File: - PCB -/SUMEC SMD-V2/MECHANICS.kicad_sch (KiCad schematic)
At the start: 8 parts, among them J1 Conn_01x04_Pin, SW1 SW_Push, SW4 SW_DPDT_x2

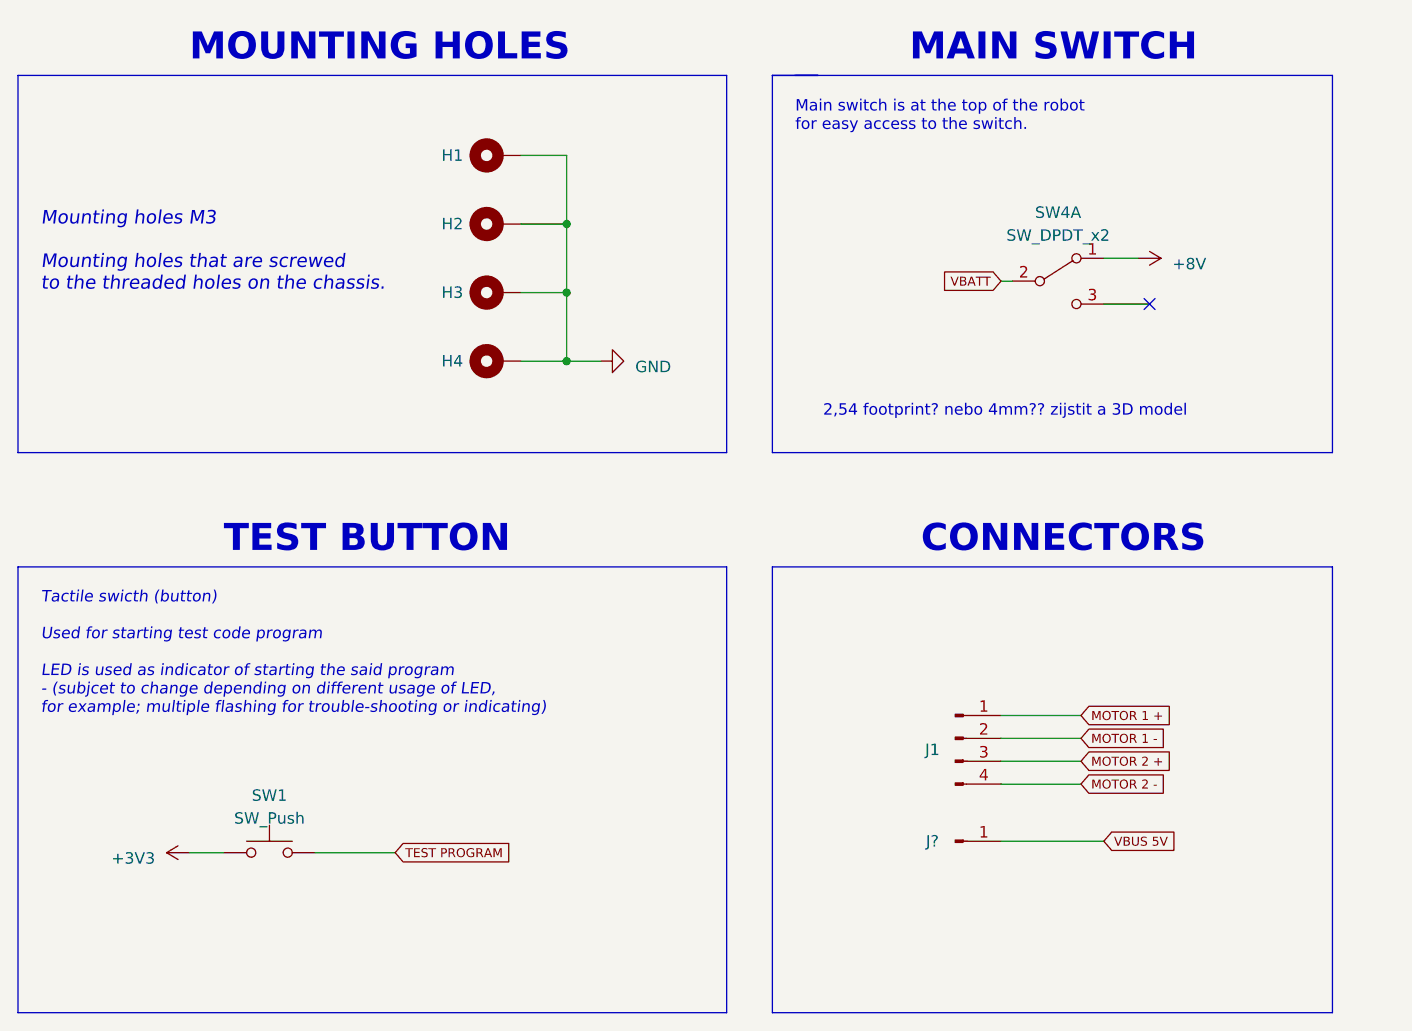
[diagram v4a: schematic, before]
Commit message: Updates:
GyroScope project file, QRE1113 Board update and BOM, SMDv2 iBOM and schematic update.
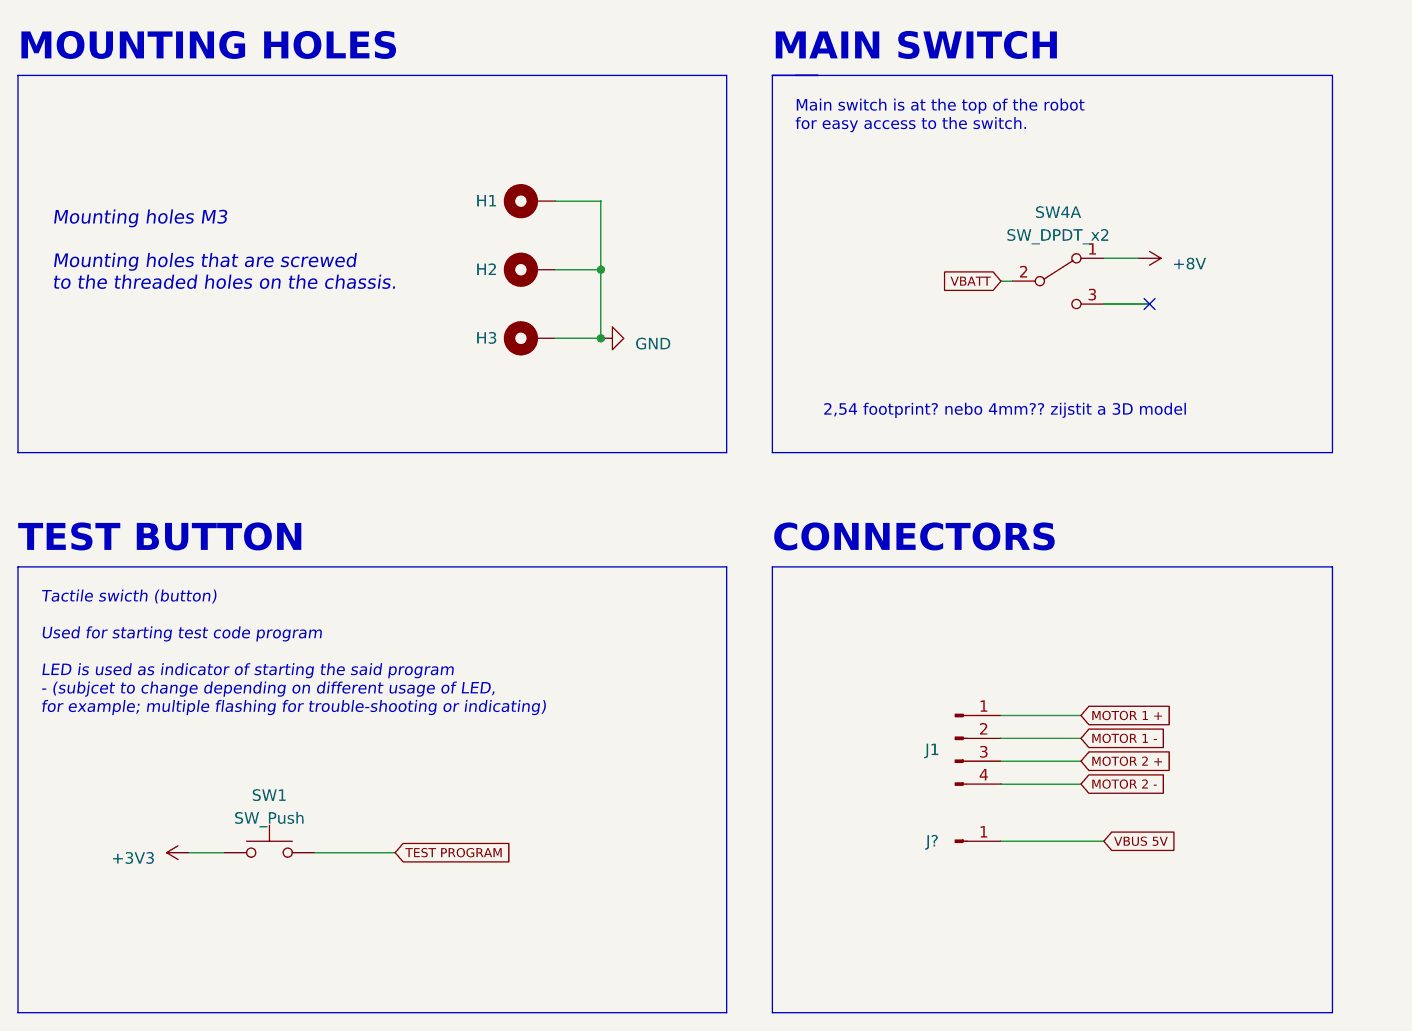
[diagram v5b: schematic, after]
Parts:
- removed H4: MountingHole_Pad, MountingHole:MountingHole_3.2mm_M3_Pad, symbol Mechanical:MountingHole_Pad
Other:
- moved on the sheet: H1, H2, H3
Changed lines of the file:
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@@
     (company "SPŠ NA PROSEKU")
   )
-  (junction (at 125.73 68.58) (diameter 0) (color 0 0 0 0)
-  )
-  (junction (at 125.73 60.96) (diameter 0) (color 0 0 0 0)
-  )
-  (junction (at 125.73 76.2) (diameter 0) (color 0 0 0 0)
+  (junction (at 129.54 73.66) (diameter 0) (color 0 0 0 0)
+  )
+  (junction (at 129.54 66.04) (diameter 0) (color 0 0 0 0)
   )
   (no_connect (at 190.5 69.85))
@@
     (stroke (width 0) (type default))
   )
-  (wire (pts (xy 120.65 76.2) (xy 125.73 76.2))
-    (stroke (width 0) (type default))
-  )
-  (wire (pts (xy 125.73 76.2) (xy 125.73 68.58))
-    (stroke (width 0) (type default))
-  )
-  (wire (pts (xy 120.65 53.34) (xy 125.73 53.34))
+  (wire (pts (xy 124.46 58.42) (xy 129.54 58.42))
     (stroke (width 0) (type default))
   )
@@
     (stroke (width 0) (type default))
   )
-  (wire (pts (xy 125.73 60.96) (xy 125.73 68.58))
+  (wire (pts (xy 129.54 66.04) (xy 129.54 73.66))
     (stroke (width 0) (type default))
   )
@@
     (stroke (width 0) (type default))
   )
-  (wire (pts (xy 125.73 68.58) (xy 120.65 68.58))
+  (wire (pts (xy 129.54 73.66) (xy 124.46 73.66))
     (stroke (width 0) (type default))
   )
@@
     (stroke (width 0) (type default))
   )
-  (wire (pts (xy 125.73 76.2) (xy 129.54 76.2))
-    (stroke (width 0) (type default))
-  )
   (polyline (pts (xy 210.82 99.06) (xy 210.82 148.59))
     (stroke (width 0) (type default))
@@
     (stroke (width 0) (type default))
   )
-  (wire (pts (xy 120.65 60.96) (xy 125.73 60.96))
+  (wire (pts (xy 124.46 66.04) (xy 129.54 66.04))
     (stroke (width 0) (type default))
   )
@@
     (stroke (width 0) (type default))
   )
-  (wire (pts (xy 125.73 53.34) (xy 125.73 60.96))
+  (wire (pts (xy 129.54 58.42) (xy 129.54 66.04))
     (stroke (width 0) (type default))
   )
@@
     (stroke (width 0) (type default))
   )
-  (text "MOUNTING HOLES" (at 83.82 43.18 0)
+  (text "MOUNTING HOLES" (at 64.77 43.18 0)
     (effects (font (size 3 3) bold (color 0 0 0 1)) (justify left bottom))
   )
   (text "Mounting holes M3 \n\nMounting holes that are screwed \nto the threaded holes on the chassis.\n"
-    (at 67.31 68.58 0)
+    (at 68.58 68.58 0)
     (effects (font (size 1.5 1.5) italic) (justify left bottom))
   )
-  (text "MAIN SWITCH" (at 163.83 43.18 0)
+  (text "MAIN SWITCH" (at 148.59 43.18 0)
     (effects (font (size 3 3) bold (color 0 0 0 1)) (justify left bottom))
   )
-  (text "TEST BUTTON" (at 87.63 97.79 0)
+  (text "TEST BUTTON" (at 64.77 97.79 0)
     (effects (font (size 3 3) bold (color 0 0 0 1)) (justify left bottom))
   )
@@
     (effects (font (size 1.27 1.27)) (justify left bottom))
   )
-  (text "CONNECTORS" (at 165.1 97.79 0)
+  (text "CONNECTORS" (at 148.59 97.79 0)
     (effects (font (size 3 3) bold (color 0 0 0 1)) (justify left bottom))
   )
@@
     )
   )
-  (symbol (lib_id "power:GND") (at 129.54 76.2 90) (unit 1)
+  (symbol (lib_id "power:GND") (at 129.54 73.66 90) (unit 1)
     (in_bom yes) (on_board yes) (dnp no) (fields_autoplaced)
-    (property "Reference" "#PWR026" (at 135.89 76.2 0)
-      (effects (font (size 1.27 1.27)) hide)
-    )
-    (property "Value" "GND" (at 133.35 76.835 90)
+    (property "Reference" "#PWR026" (at 135.89 73.66 0)
+      (effects (font (size 1.27 1.27)) hide)
+    )
+    (property "Value" "GND" (at 133.35 74.295 90)
       (effects (font (size 1.27 1.27)) (justify right))
     )
-    (property "Footprint" "" (at 129.54 76.2 0)
-      (effects (font (size 1.27 1.27)) hide)
-    )
-    (property "Datasheet" "" (at 129.54 76.2 0)
+    (property "Footprint" "" (at 129.54 73.66 0)
+      (effects (font (size 1.27 1.27)) hide)
+    )
+    (property "Datasheet" "" (at 129.54 73.66 0)
       (effects (font (size 1.27 1.27)) hide)
     )
@@
     )
   )
-  (symbol (lib_id "Mechanical:MountingHole_Pad") (at 118.11 76.2 90) (unit 1)
-    (in_bom yes) (on_board yes) (dnp no)
-    (property "Reference" "H4" (at 113.03 76.2 90)
-      (effects (font (size 1.27 1.27)))
-    )
-    (property "Value" "MountingHole_Pad" (at 116.84 73.66 90)
-      (effects (font (size 1.27 1.27)) hide)
-    )
-    (property "Footprint" "MountingHole:MountingHole_3.2mm_M3_Pad" (at 118.11 76.2 0)
-      (effects (font (size 1.27 1.27)) hide)
-    )
-    (property "Datasheet" "~" (at 118.11 76.2 0)
-      (effects (font (size 1.27 1.27)) hide)
-    )
-    (pin "1")
-    (instances
-      (project "sumec"
-        (path "/fc70a1a8-ed7c-4a0f-9b1a-f23293528385/05a35bad-c108-46ad-8f95-76319a60a14f"
-          (reference "H4") (unit 1)
-        )
-      )
-    )
-  )
   (symbol (lib_id "Connector:Conn_01x01_Pin") (at 168.91 129.54 0) (unit 1)
     (in_bom yes) (on_board yes) (dnp no)
@@
     )
   )
-  (symbol (lib_id "Mechanical:MountingHole_Pad") (at 118.11 53.34 90) (unit 1)
-    (in_bom yes) (on_board yes) (dnp no)
-    (property "Reference" "H1" (at 113.03 53.34 90)
-      (effects (font (size 1.27 1.27)))
-    )
-    (property "Value" "MountingHole_Pad" (at 116.84 50.8 90)
-      (effects (font (size 1.27 1.27)) hide)
-    )
-    (property "Footprint" "MountingHole:MountingHole_3.2mm_M3_Pad" (at 118.11 53.34 0)
-      (effects (font (size 1.27 1.27)) hide)
-    )
-    (property "Datasheet" "~" (at 118.11 53.34 0)
+  (symbol (lib_id "Mechanical:MountingHole_Pad") (at 121.92 58.42 90) (unit 1)
+    (in_bom yes) (on_board yes) (dnp no)
+    (property "Reference" "H1" (at 116.84 58.42 90)
+      (effects (font (size 1.27 1.27)))
+    )
+    (property "Value" "MountingHole_Pad" (at 120.65 55.88 90)
+      (effects (font (size 1.27 1.27)) hide)
+    )
+    (property "Footprint" "MountingHole:MountingHole_3.2mm_M3_Pad" (at 121.92 58.42 0)
+      (effects (font (size 1.27 1.27)) hide)
+    )
+    (property "Datasheet" "~" (at 121.92 58.42 0)
       (effects (font (size 1.27 1.27)) hide)
     )
@@
     )
   )
-  (symbol (lib_id "Mechanical:MountingHole_Pad") (at 118.11 60.96 90) (unit 1)
-    (in_bom yes) (on_board yes) (dnp no)
-    (property "Reference" "H2" (at 113.03 60.96 90)
-      (effects (font (size 1.27 1.27)))
-    )
-    (property "Value" "MountingHole_Pad" (at 116.84 58.42 90)
-      (effects (font (size 1.27 1.27)) hide)
-    )
-    (property "Footprint" "MountingHole:MountingHole_3.2mm_M3_Pad" (at 118.11 60.96 0)
-      (effects (font (size 1.27 1.27)) hide)
-    )
-    (property "Datasheet" "~" (at 118.11 60.96 0)
+  (symbol (lib_id "Mechanical:MountingHole_Pad") (at 121.92 66.04 90) (unit 1)
+    (in_bom yes) (on_board yes) (dnp no)
+    (property "Reference" "H2" (at 116.84 66.04 90)
+      (effects (font (size 1.27 1.27)))
+    )
+    (property "Value" "MountingHole_Pad" (at 120.65 63.5 90)
+      (effects (font (size 1.27 1.27)) hide)
+    )
+    (property "Footprint" "MountingHole:MountingHole_3.2mm_M3_Pad" (at 121.92 66.04 0)
+      (effects (font (size 1.27 1.27)) hide)
+    )
+    (property "Datasheet" "~" (at 121.92 66.04 0)
       (effects (font (size 1.27 1.27)) hide)
     )
@@
     )
   )
-  (symbol (lib_id "Mechanical:MountingHole_Pad") (at 118.11 68.58 90) (unit 1)
-    (in_bom yes) (on_board yes) (dnp no)
-    (property "Reference" "H3" (at 113.03 68.58 90)
-      (effects (font (size 1.27 1.27)))
-    )
-    (property "Value" "MountingHole_Pad" (at 116.84 66.04 90)
-      (effects (font (size 1.27 1.27)) hide)
-    )
-    (property "Footprint" "MountingHole:MountingHole_3.2mm_M3_Pad" (at 118.11 68.58 0)
-      (effects (font (size 1.27 1.27)) hide)
-    )
-    (property "Datasheet" "~" (at 118.11 68.58 0)
-      (effects (font (size 1.27 1.27)) hide)
-    )
+  (symbol (lib_id "Mechanical:MountingHole_Pad") (at 121.92 73.66 90) (unit 1)
+    (in_bom yes) (on_board yes) (dnp no)
+    (property "Reference" "H3" (at 116.84 73.66 90)
+      (effects (font (size 1.27 1.27)))
+    )
+    (property "Value" "MountingHole_Pad" (at 120.65 71.12 90)
+      (effects (font (size 1.27 1.27)) hide)
+    )
+    (property "Footprint" "MountingHole:MountingHole_3.2mm_M3_Pad" (at 121.92 73.66 0)
+      (effects (font (size 1.27 1.27)) hide)
+    )
+    (property "Datasheet" "~" (at 121.92 73.66 0)
+      (effects (font (size 1.27 1.27)) hide)
+    )

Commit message: SMDv2 Schematic update
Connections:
- net MOTOR 1 + renamed OUT 1A
- net MOTOR 1 - renamed OUT 1B
- net MOTOR 2 + renamed OUT 2A
- net MOTOR 2 - renamed OUT 2B
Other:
- note added: "4mm custom footprint"
- note removed: "2,54 footprint? nebo 4mm?? zijstit a 3D model"
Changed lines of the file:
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@@
+    (stroke (width 0) (type default))
+  )
+  (wire (pts (xy 132.08 73.66) (xy 129.54 73.66))
     (stroke (width 0) (type default))
   )
@@
     (stroke (width 0) (type default))
   )
-  (wire (pts (xy 185.42 129.54) (xy 173.99 129.54))
+  (wire (pts (xy 182.88 129.54) (xy 173.99 129.54))
     (stroke (width 0) (type default))
   )
@@
     (effects (font (size 1.27 1.27) italic) (justify left bottom))
   )
-  (text " 2,54 footprint? nebo 4mm?? zijstit a 3D model" (at 153.67 82.55 0)
+  (text " 4mm custom footprint" (at 167.64 78.74 0)
     (effects (font (size 1.27 1.27) (color 255 0 0 1)) (justify left bottom))
   )
-  (global_label "VBUS 5V" (shape input) (at 185.42 129.54 0) (fields_autoplaced)
+  (global_label "OUT 2B" (shape input) (at 182.88 123.19 0) (fields_autoplaced)
     (effects (font (size 1 1) (color 0 0 0 1)) (justify left))
-    (property "Intersheetrefs" "${INTERSHEET_REFS}" (at 194.1364 129.54 0)
+    (property "Intersheetrefs" "${INTERSHEET_REFS}" (at 190.7393 123.19 0)
       (effects (font (size 1.27 1.27)) (justify left) hide)
     )
   )
-  (global_label "MOTOR 2 -" (shape input) (at 182.88 123.19 0) (fields_autoplaced)
+  (global_label "VBUS 5V" (shape input) (at 182.88 129.54 0) (fields_autoplaced)
     (effects (font (size 1 1) (color 0 0 0 1)) (justify left))
-    (property "Intersheetrefs" "${INTERSHEET_REFS}" (at 193.8822 123.19 0)
+    (property "Intersheetrefs" "${INTERSHEET_REFS}" (at 191.5964 129.54 0)
       (effects (font (size 1.27 1.27)) (justify left) hide)
     )
   )
-  (global_label "MOTOR 1 -" (shape input) (at 182.88 118.11 0) (fields_autoplaced)
+  (global_label "OUT 1B" (shape input) (at 182.88 118.11 0) (fields_autoplaced)
     (effects (font (size 1 1) (color 0 0 0 1)) (justify left))
-    (property "Intersheetrefs" "${INTERSHEET_REFS}" (at 193.8822 118.11 0)
+    (property "Intersheetrefs" "${INTERSHEET_REFS}" (at 190.7393 118.11 0)
       (effects (font (size 1.27 1.27)) (justify left) hide)
     )
   )
-  (global_label "MOTOR 2 +" (shape input) (at 182.88 120.65 0) (fields_autoplaced)
+  (global_label "OUT 1A" (shape input) (at 182.88 115.57 0) (fields_autoplaced)
     (effects (font (size 1 1) (color 0 0 0 1)) (justify left))
-    (property "Intersheetrefs" "${INTERSHEET_REFS}" (at 193.8822 120.65 0)
+    (property "Intersheetrefs" "${INTERSHEET_REFS}" (at 190.5964 115.57 0)
+      (effects (font (size 1.27 1.27)) (justify left) hide)
+    )
+  )
+  (global_label "OUT 2A" (shape input) (at 182.88 120.65 0) (fields_autoplaced)
+    (effects (font (size 1 1) (color 0 0 0 1)) (justify left))
+    (property "Intersheetrefs" "${INTERSHEET_REFS}" (at 190.5964 120.65 0)
       (effects (font (size 1.27 1.27)) (justify left) hide)
     )
@@
     )
   )
-  (global_label "MOTOR 1 +" (shape input) (at 182.88 115.57 0) (fields_autoplaced)
-    (effects (font (size 1 1) (color 0 0 0 1)) (justify left))
-    (property "Intersheetrefs" "${INTERSHEET_REFS}" (at 193.8822 115.57 0)
-      (effects (font (size 1.27 1.27)) (justify left) hide)
-    )
-  )
-  (symbol (lib_id "power:GND") (at 129.54 73.66 90) (unit 1)
+  (symbol (lib_id "power:GND") (at 132.08 73.66 90) (unit 1)
     (in_bom yes) (on_board yes) (dnp no) (fields_autoplaced)
-    (property "Reference" "#PWR026" (at 135.89 73.66 0)
+    (property "Reference" "#PWR026" (at 138.43 73.66 0)
       (effects (font (size 1.27 1.27)) hide)
     )
-    (property "Value" "GND" (at 133.35 74.295 90)
+    (property "Value" "GND" (at 135.89 74.295 90)
       (effects (font (size 1.27 1.27)) (justify right))
     )
-    (property "Footprint" "" (at 129.54 73.66 0)
+    (property "Footprint" "" (at 132.08 73.66 0)
       (effects (font (size 1.27 1.27)) hide)
     )
-    (property "Datasheet" "" (at 129.54 73.66 0)
+    (property "Datasheet" "" (at 132.08 73.66 0)
       (effects (font (size 1.27 1.27)) hide)
     )

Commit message: schematic miniupdate
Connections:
- net +8V renamed +12V
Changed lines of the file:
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@@
+    )
+  )
+  (symbol (lib_id "power:+12V") (at 189.23 64.77 270) (unit 1)
+    (in_bom yes) (on_board yes) (dnp no) (fields_autoplaced)
+    (property "Reference" "#PWR06" (at 185.42 64.77 0)
+      (effects (font (size 1.27 1.27)) hide)
+    )
+    (property "Value" "+12V" (at 193.04 65.405 90)
+      (effects (font (size 1.27 1.27)) (justify left))
+    )
+    (property "Footprint" "" (at 189.23 64.77 0)
+      (effects (font (size 1.27 1.27)) hide)
+    )
+    (property "Datasheet" "" (at 189.23 64.77 0)
+      (effects (font (size 1.27 1.27)) hide)
+    )
+    (pin "1")
+    (instances
+      (project "sumec"
+        (path "/fc70a1a8-ed7c-4a0f-9b1a-f23293528385/05a35bad-c108-46ad-8f95-76319a60a14f"
+          (reference "#PWR06") (unit 1)
+        )
+      )
     )
   )
@@
         )
       )
-    )
-  )
-  (symbol (lib_id "power:+8V") (at 189.23 64.77 270) (unit 1)
-    (in_bom yes) (on_board yes) (dnp no) (fields_autoplaced)
-    (property "Reference" "#PWR048" (at 185.42 64.77 0)
-      (effects (font (size 1.27 1.27)) hide)
-    )
-    (property "Value" "+8V" (at 193.04 65.405 90)
-      (effects (font (size 1.27 1.27)) (justify left))
-    )
-    (property "Footprint" "" (at 189.23 64.77 0)
-      (effects (font (size 1.27 1.27)) hide)
-    )
-    (property "Datasheet" "" (at 189.23 64.77 0)
-      (effects (font (size 1.27 1.27)) hide)
-    )
-    (pin "1")
-    (instances
-      (project "sumec"
-        (path "/fc70a1a8-ed7c-4a0f-9b1a-f23293528385/05a35bad-c108-46ad-8f95-76319a60a14f"
-          (reference "#PWR048") (unit 1)
-        )
-        (path "/fc70a1a8-ed7c-4a0f-9b1a-f23293528385/11aa20d4-c4ff-49be-9179-c2911da50f67"
-          (reference "#PWR047") (unit 1)
-        )
-      )

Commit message: New switch
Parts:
- SW4: footprint sumec-smdV2_library:Custom_SPDT_Switch -> sumec-smdV2_library:Custom_SPDT_4.8mm_Switch
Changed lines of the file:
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@@
       (effects (font (size 1.27 1.27)))
     )
-    (property "Footprint" "sumec-smdV2_library:Custom_SPDT_Switch" (at 180.34 67.31 0)
+    (property "Footprint" "sumec-smdV2_library:Custom_SPDT_4.8mm_Switch" (at 180.34 67.31 0)
       (effects (font (size 1.27 1.27)) hide)
     )
